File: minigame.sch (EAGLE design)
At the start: 37 parts, among them J1 AVR_SPI_PRG_6PTH, U1 MCP73831, U2 MIC5219 3.3V, Y1 8MHz

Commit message: ERC
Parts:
- LED1: value (none) -> RED
- OLED128X64: value (none) -> ADAFRUIT-938
- POWER: value (none) -> ON/OFF
- renumbered OLED128X64-938 to OLED128X64
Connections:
- removed net N$3: R1.1, S1.2, U$1.!RESET
- net GND: now also BAT1.-; no longer BAT1.+
- net RST: now also R1.1, S1.2, U$1.!RESET
- net VBAT: now also BAT1.+; no longer BAT1.-
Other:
- moved on the sheet: BAT1

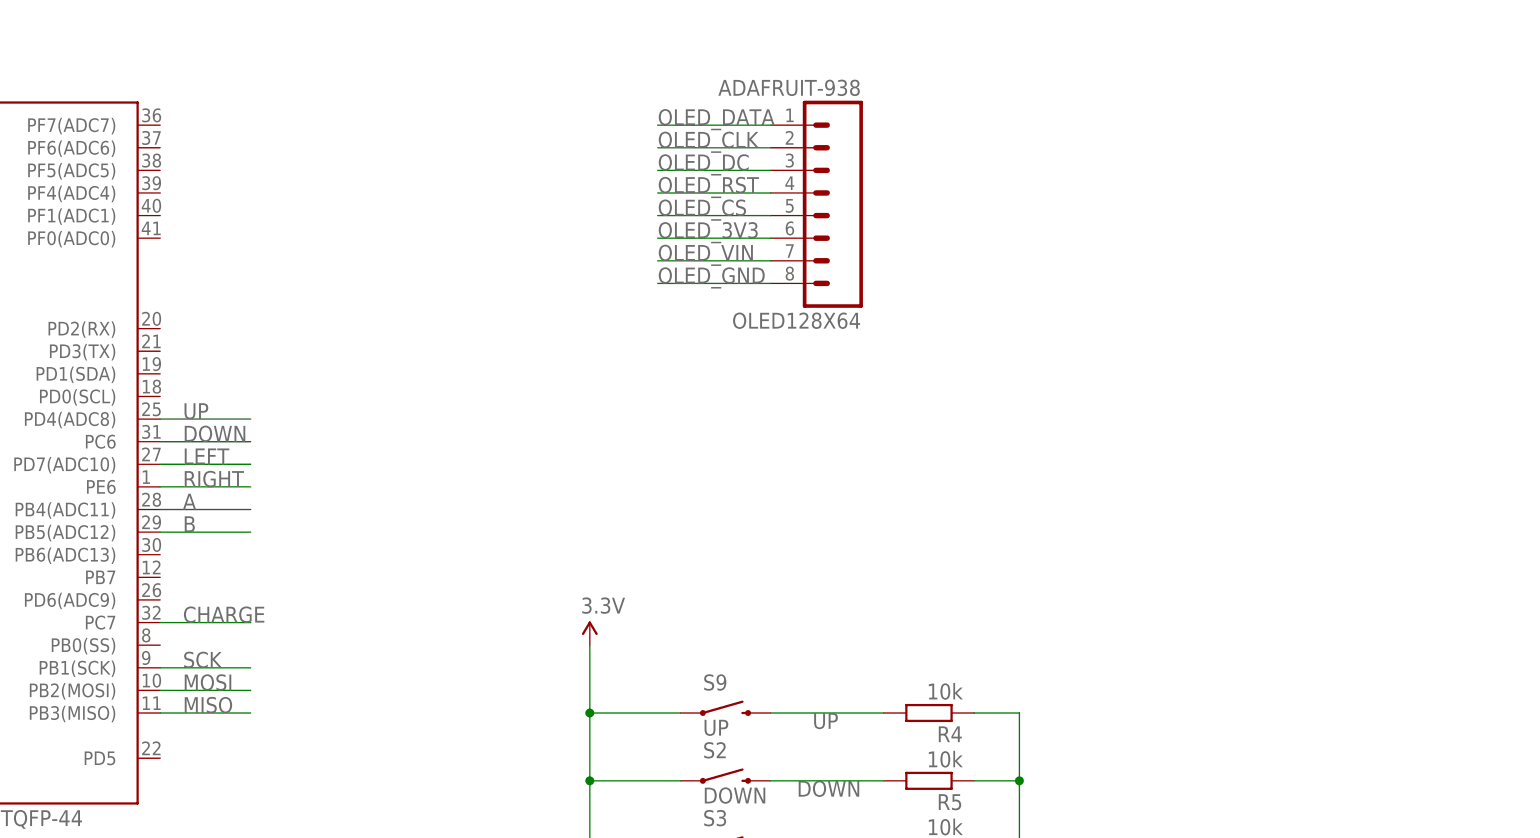
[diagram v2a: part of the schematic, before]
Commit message: Added OLED wires Added buzzer circuit
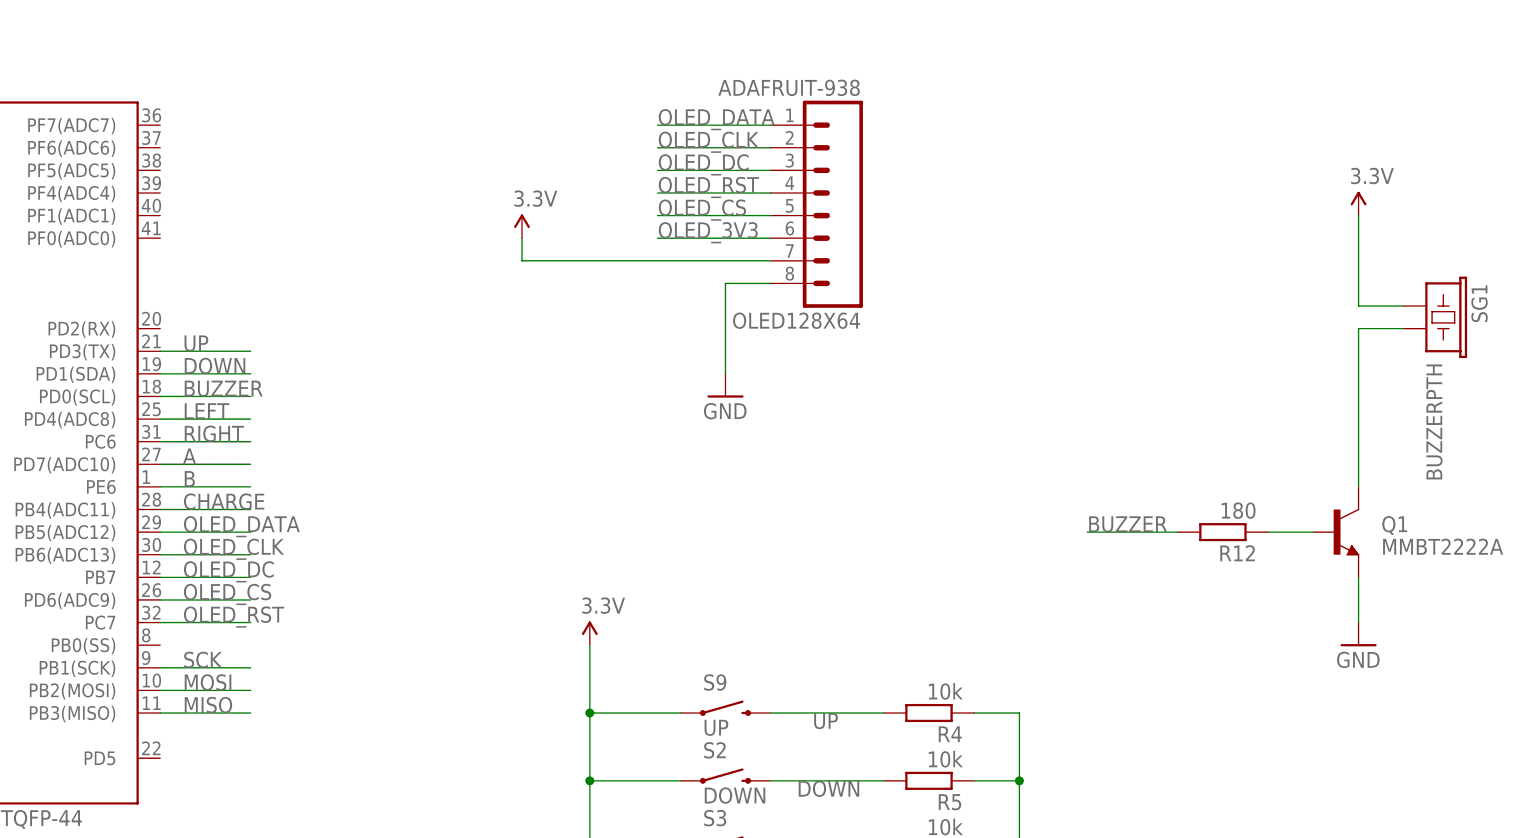
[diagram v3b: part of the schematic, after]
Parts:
- added Q1: MMBT2222A, SparkFun-DiscreteSemi:TRANSISTOR_NPNMMBT2222A
- added R12: 180, rcl:R-EU_M0805
- added SG1: BUZZERPTH, SparkFun-Electromechanical:BUZZERPTH
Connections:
- removed net OLED_GND: OLED128X64.8
- removed net OLED_VIN: OLED128X64.7
- new net BUZZER: R12.2, U$1.PD0(SCL)
- new net N$11: Q1.B, R12.1
- new net N$3: Q1.C, SG1.2
- net 3.3V: now also OLED128X64.7, SG1.1
- net A: now also U$1.PD7(ADC10); no longer U$1.PB4(ADC11)
- net B: now also U$1.PE6; no longer U$1.PB5(ADC12)
- net CHARGE: now also U$1.PB4(ADC11); no longer U$1.PC7
- net DOWN: now also U$1.PD1(SDA); no longer U$1.PC6
- net GND: now also OLED128X64.8, Q1.E
- net LEFT: now also U$1.PD4(ADC8); no longer U$1.PD7(ADC10)
- net OLED_CLK: now also U$1.PB6(ADC13)
- net OLED_CS: now also U$1.PD6(ADC9)
- net OLED_DATA: now also U$1.PB5(ADC12)
- net OLED_DC: now also U$1.PB7
- net OLED_RST: now also U$1.PC7
- net RIGHT: now also U$1.PC6; no longer U$1.PE6
- net UP: now also U$1.PD3(TX); no longer U$1.PD4(ADC8)
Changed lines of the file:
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@@
 <part name="U$1" library="SparkFun-DigitalIC" deviceset="ATMEGA32U4" device="TQFP-44"/>
 <part name="SUPPLY1" library="SparkFun-Aesthetics" deviceset="3.3V" device=""/>
-<part name="GND1" library="SparkFun-Aesthetics" deviceset="GND" device=""/>
+<part name="COPY+" library="SparkFun-Aesthetics" deviceset="GND" device=""/>
 <part name="JP1" library="SparkFun-Connectors" deviceset="USB" device="-SMD-NS"/>
 <part name="Y1" library="SparkFun-FreqCtrl" deviceset="CRYSTAL" device="HC49US" value="8MHz"/>
@@
 <part name="C9" library="SparkFun-Passives" deviceset="CAP" device="1206" value="0.1uF"/>
 <part name="SUPPLY5" library="SparkFun-Aesthetics" deviceset="3.3V" device=""/>
+<part name="COPY+1" library="SparkFun-Aesthetics" deviceset="GND" device=""/>
+<part name="SUPPLY6" library="SparkFun-Aesthetics" deviceset="3.3V" device=""/>
+<part name="SG1" library="SparkFun-Electromechanical" deviceset="BUZZER" device="PTH"/>
+<part name="Q1" library="SparkFun-DiscreteSemi" deviceset="TRANSISTOR_NPN" device="MMBT2222A" value="MMBT2222A"/>
+<part name="R12" library="rcl" deviceset="R-EU_" device="M0805" value="180"/>
+<part name="SUPPLY7" library="SparkFun-Aesthetics" deviceset="3.3V" device=""/>
+<part name="COPY+2" library="SparkFun-Aesthetics" deviceset="GND" device=""/>
 </parts>
 <sheets>
@@
 <instance part="U$1" gate="G$1" x="15.24" y="40.64"/>
 <instance part="SUPPLY1" gate="G$1" x="-30.48" y="99.06"/>
-<instance part="GND1" gate="1" x="-7.62" y="-10.16"/>
+<instance part="COPY+" gate="1" x="-7.62" y="-10.16"/>
 <instance part="JP1" gate="G$1" x="-81.28" y="76.2" rot="R180"/>
 <instance part="Y1" gate="G$1" x="-10.16" y="27.94" rot="R90"/>
@@
 <instance part="C9" gate="G$1" x="152.4" y="-76.2" rot="R180"/>
 <instance part="SUPPLY5" gate="G$1" x="152.4" y="-63.5"/>
+<instance part="COPY+1" gate="1" x="96.52" y="45.72"/>
+<instance part="SUPPLY6" gate="G$1" x="73.66" y="63.5"/>
+<instance part="SG1" gate="G$1" x="175.26" y="55.88" rot="R270"/>
+<instance part="Q1" gate="G$1" x="165.1" y="30.48"/>
+<instance part="R12" gate="G$1" x="152.4" y="30.48" rot="R180"/>
+<instance part="SUPPLY7" gate="G$1" x="167.64" y="66.04"/>
+<instance part="COPY+2" gate="1" x="167.64" y="17.78"/>
 </instances>
 <busses>
@@
 <junction x="-7.62" y="7.62"/>
 <junction x="-7.62" y="5.08"/>
-<pinref part="GND1" gate="1" pin="GND"/>
+<pinref part="COPY+" gate="1" pin="GND"/>
 <wire x1="-7.62" y1="-7.62" x2="-7.62" y2="2.54" width="0.1524" layer="91"/>
 <junction x="-7.62" y="2.54"/>
@@
 <wire x1="35.56" y1="-86.36" x2="35.56" y2="-93.98" width="0.1524" layer="91"/>
 </segment>
+<segment>
+<pinref part="COPY+1" gate="1" pin="GND"/>
+<wire x1="96.52" y1="48.26" x2="96.52" y2="58.42" width="0.1524" layer="91"/>
+<pinref part="OLED128X64" gate="G$1" pin="8"/>
+<wire x1="96.52" y1="58.42" x2="101.6" y2="58.42" width="0.1524" layer="91"/>
+</segment>
+<segment>
+<pinref part="COPY+2" gate="1" pin="GND"/>
+<pinref part="Q1" gate="G$1" pin="E"/>
+<wire x1="167.64" y1="20.32" x2="167.64" y2="25.4" width="0.1524" layer="91"/>
+</segment>
 </net>
 <net name="3.3V" class="0">
@@
 <junction x="152.4" y="-68.58"/>
 </segment>
+<segment>
+<pinref part="OLED128X64" gate="G$1" pin="7"/>
+<wire x1="101.6" y1="60.96" x2="73.66" y2="60.96" width="0.1524" layer="91"/>
+<pinref part="SUPPLY6" gate="G$1" pin="3.3V"/>
+<wire x1="73.66" y1="60.96" x2="73.66" y2="63.5" width="0.1524" layer="91"/>
+</segment>
+<segment>
+<pinref part="SUPPLY7" gate="G$1" pin="3.3V"/>
+<wire x1="167.64" y1="66.04" x2="167.64" y2="55.88" width="0.1524" layer="91"/>
+<pinref part="SG1" gate="G$1" pin="1"/>
+<wire x1="167.64" y1="55.88" x2="172.72" y2="55.88" width="0.1524" layer="91"/>
+</segment>
 </net>
 <net name="N$4" class="0">
@@
 <label x="88.9" y="76.2" size="1.778" layer="95"/>
 </segment>
+<segment>
+<pinref part="U$1" gate="G$1" pin="PB5(ADC12)"/>
+<wire x1="33.02" y1="30.48" x2="43.18" y2="30.48" width="0.1524" layer="91"/>
+<label x="35.56" y="30.48" size="1.778" layer="95"/>
+</segment>
 </net>
 <net name="OLED_CLK" class="0">
@@
 <label x="88.9" y="73.66" size="1.778" layer="95"/>
 </segment>
+<segment>
+<pinref part="U$1" gate="G$1" pin="PB6(ADC13)"/>
+<wire x1="33.02" y1="27.94" x2="43.18" y2="27.94" width="0.1524" layer="91"/>
+<label x="35.56" y="27.94" size="1.778" layer="95"/>
+</segment>
 </net>
 <net name="OLED_DC" class="0">
@@
 <label x="88.9" y="71.12" size="1.778" layer="95"/>
 </segment>
+<segment>
+<pinref part="U$1" gate="G$1" pin="PB7"/>
+<wire x1="33.02" y1="25.4" x2="43.18" y2="25.4" width="0.1524" layer="91"/>
+<label x="35.56" y="25.4" size="1.778" layer="95"/>
+</segment>
 </net>
 <net name="OLED_RST" class="0">
@@
 <label x="88.9" y="68.58" size="1.778" layer="95"/>
 </segment>
+<segment>
+<pinref part="U$1" gate="G$1" pin="PC7"/>
+<wire x1="33.02" y1="20.32" x2="43.18" y2="20.32" width="0.1524" layer="91"/>
+<label x="35.56" y="20.32" size="1.778" layer="95"/>
+</segment>
 </net>
 <net name="OLED_CS" class="0">
@@
 <label x="88.9" y="66.04" size="1.778" layer="95"/>
 </segment>
+<segment>
+<pinref part="U$1" gate="G$1" pin="PD6(ADC9)"/>
+<wire x1="33.02" y1="22.86" x2="43.18" y2="22.86" width="0.1524" layer="91"/>
+<label x="35.56" y="22.86" size="1.778" layer="95"/>
+</segment>
 </net>
 <net name="OLED_3V3" class="0">
@@
 <wire x1="101.6" y1="63.5" x2="88.9" y2="63.5" width="0.1524" layer="91"/>
 <label x="88.9" y="63.5" size="1.778" layer="95"/>
-</segment>
-</net>
-<net name="OLED_VIN" class="0">
-<segment>
-<pinref part="OLED128X64" gate="G$1" pin="7"/>
-<wire x1="101.6" y1="60.96" x2="88.9" y2="60.96" width="0.1524" layer="91"/>
-<label x="88.9" y="60.96" size="1.778" layer="95"/>
-</segment>
-</net>
-<net name="OLED_GND" class="0">
-<segment>
-<pinref part="OLED128X64" gate="G$1" pin="8"/>
-<wire x1="101.6" y1="58.42" x2="88.9" y2="58.42" width="0.1524" layer="91"/>
-<label x="88.9" y="58.42" size="1.778" layer="95"/>
 </segment>
 </net>
@@
 </segment>
 <segment>
-<pinref part="U$1" gate="G$1" pin="PD4(ADC8)"/>
-<wire x1="33.02" y1="43.18" x2="43.18" y2="43.18" width="0.1524" layer="91"/>
-<label x="35.56" y="43.18" size="1.778" layer="95"/>
+<pinref part="U$1" gate="G$1" pin="PD3(TX)"/>
+<wire x1="33.02" y1="50.8" x2="43.18" y2="50.8" width="0.1524" layer="91"/>
+<label x="35.56" y="50.8" size="1.778" layer="95"/>
 </segment>
 </net>
@@
 </segment>
 <segment>
-<pinref part="U$1" gate="G$1" pin="PC6"/>
-<wire x1="33.02" y1="40.64" x2="43.18" y2="40.64" width="0.1524" layer="91"/>
-<label x="35.56" y="40.64" size="1.778" layer="95"/>
+<pinref part="U$1" gate="G$1" pin="PD1(SDA)"/>
+<wire x1="33.02" y1="48.26" x2="43.18" y2="48.26" width="0.1524" layer="91"/>
+<label x="35.56" y="48.26" size="1.778" layer="95"/>
 </segment>
 </net>
@@
 </segment>
 <segment>
-<pinref part="U$1" gate="G$1" pin="PD7(ADC10)"/>
-<wire x1="33.02" y1="38.1" x2="43.18" y2="38.1" width="0.1524" layer="91"/>
-<label x="35.56" y="38.1" size="1.778" layer="95"/>
+<pinref part="U$1" gate="G$1" pin="PD4(ADC8)"/>
+<wire x1="33.02" y1="43.18" x2="43.18" y2="43.18" width="0.1524" layer="91"/>
+<label x="35.56" y="43.18" size="1.778" layer="95"/>
 </segment>
 </net>
@@
 </segment>
 <segment>
-<pinref part="U$1" gate="G$1" pin="PE6"/>
-<wire x1="33.02" y1="35.56" x2="43.18" y2="35.56" width="0.1524" layer="91"/>
-<label x="35.56" y="35.56" size="1.778" layer="95"/>
+<pinref part="U$1" gate="G$1" pin="PC6"/>
+<wire x1="33.02" y1="40.64" x2="43.18" y2="40.64" width="0.1524" layer="91"/>
+<label x="35.56" y="40.64" size="1.778" layer="95"/>
 </segment>
 </net>
@@
 </segment>
 <segment>
-<pinref part="U$1" gate="G$1" pin="PB4(ADC11)"/>
-<wire x1="33.02" y1="33.02" x2="43.18" y2="33.02" width="0.1524" layer="91"/>
-<label x="35.56" y="33.02" size="1.778" layer="95"/>
+<pinref part="U$1" gate="G$1" pin="PD7(ADC10)"/>
+<wire x1="33.02" y1="38.1" x2="43.18" y2="38.1" width="0.1524" layer="91"/>
+<label x="35.56" y="38.1" size="1.778" layer="95"/>
 </segment>
 </net>
@@
 </segment>
 <segment>
-<pinref part="U$1" gate="G$1" pin="PB5(ADC12)"/>
-<wire x1="33.02" y1="30.48" x2="43.18" y2="30.48" width="0.1524" layer="91"/>
-<label x="35.56" y="30.48" size="1.778" layer="95"/>
+<pinref part="U$1" gate="G$1" pin="PE6"/>
+<wire x1="33.02" y1="35.56" x2="43.18" y2="35.56" width="0.1524" layer="91"/>
+<label x="35.56" y="35.56" size="1.778" layer="95"/>
 </segment>
 </net>
@@
 </net>
 <net name="CHARGE" class="0">
-<segment>
-<pinref part="U$1" gate="G$1" pin="PC7"/>
-<wire x1="33.02" y1="20.32" x2="43.18" y2="20.32" width="0.1524" layer="91"/>
-<label x="35.56" y="20.32" size="1.778" layer="95"/>
-</segment>
 <segment>
 <pinref part="U1" gate="G$1" pin="STAT"/>
@@
 <junction x="-25.4" y="-33.02"/>
 <label x="-22.86" y="-33.02" size="1.778" layer="95"/>
+</segment>
+<segment>
+<pinref part="U$1" gate="G$1" pin="PB4(ADC11)"/>
+<wire x1="33.02" y1="33.02" x2="43.18" y2="33.02" width="0.1524" layer="91"/>
+<label x="35.56" y="33.02" size="1.778" layer="95"/>
 </segment>
 </net>
@@
 </segment>
 </net>
+<net name="N$3" class="0">
+<segment>
+<pinref part="SG1" gate="G$1" pin="2"/>
+<wire x1="172.72" y1="53.34" x2="167.64" y2="53.34" width="0.1524" layer="91"/>
+<pinref part="Q1" gate="G$1" pin="C"/>
+<wire x1="167.64" y1="53.34" x2="167.64" y2="35.56" width="0.1524" layer="91"/>
+</segment>
+</net>
+<net name="N$11" class="0">
+<segment>
+<pinref part="R12" gate="G$1" pin="1"/>
+<pinref part="Q1" gate="G$1" pin="B"/>
+<wire x1="157.48" y1="30.48" x2="162.56" y2="30.48" width="0.1524" layer="91"/>
+</segment>
+</net>
+<net name="BUZZER" class="0">
+<segment>
+<pinref part="U$1" gate="G$1" pin="PD0(SCL)"/>
+<wire x1="33.02" y1="45.72" x2="43.18" y2="45.72" width="0.1524" layer="91"/>
+<label x="35.56" y="45.72" size="1.778" layer="95"/>
+</segment>
+<segment>
+<pinref part="R12" gate="G$1" pin="2"/>
+<wire x1="147.32" y1="30.48" x2="137.16" y2="30.48" width="0.1524" layer="91"/>
+<label x="137.16" y="30.48" size="1.778" layer="95"/>
+</segment>
+</net>

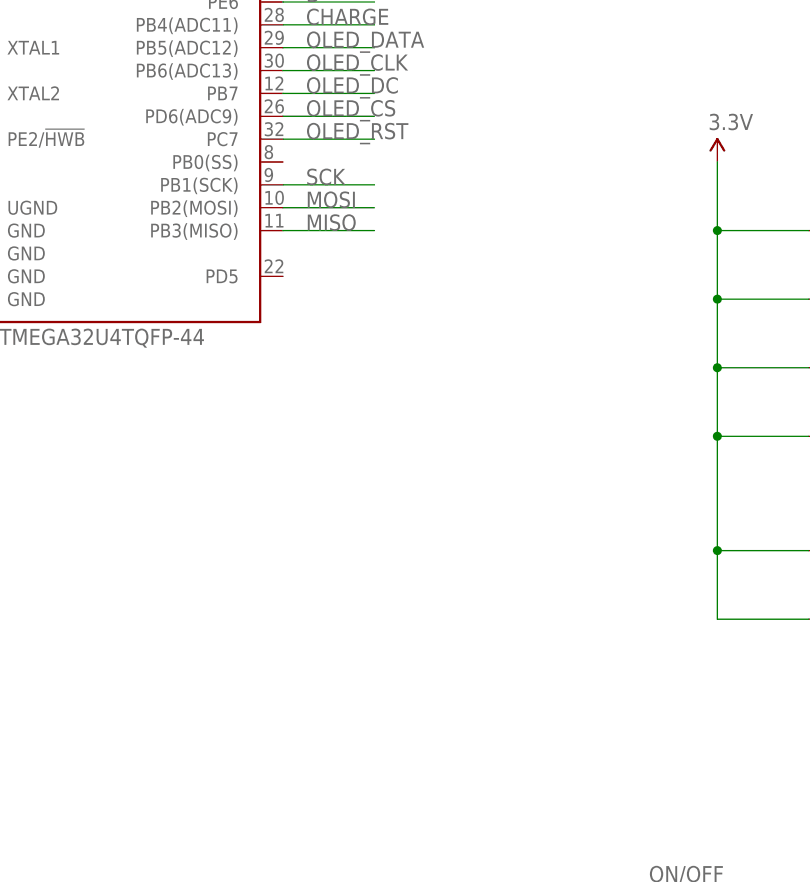
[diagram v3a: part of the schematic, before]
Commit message: Added RX/TX LEDs
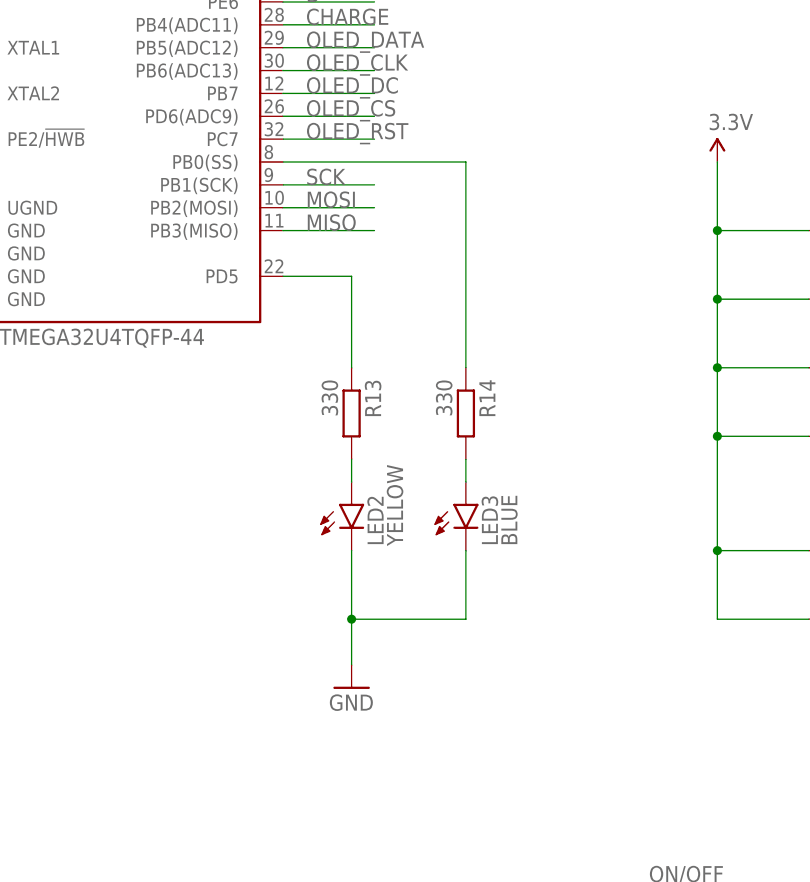
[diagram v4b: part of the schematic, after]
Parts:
- added LED2: YELLOW, SparkFun-LED:LED0603
- added LED3: BLUE, SparkFun-LED:LED0603
- added R13, R14: 330, rcl:R-EU_M0805
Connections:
- new net N$12: LED2.A, R13.2
- new net N$13: LED3.A, R14.2
- new net N$15: R13.1, U$1.PD5
- new net N$16: R14.1, U$1.PB0(SS)
- net GND: now also LED2.C, LED3.C
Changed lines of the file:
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@@
 <part name="SUPPLY7" library="SparkFun-Aesthetics" deviceset="3.3V" device=""/>
 <part name="COPY+2" library="SparkFun-Aesthetics" deviceset="GND" device=""/>
+<part name="LED2" library="SparkFun-LED" deviceset="LED" device="0603" value="YELLOW"/>
+<part name="LED3" library="SparkFun-LED" deviceset="LED" device="0603" value="BLUE"/>
+<part name="R13" library="rcl" deviceset="R-EU_" device="M0805" value="330"/>
+<part name="R14" library="rcl" deviceset="R-EU_" device="M0805" value="330"/>
+<part name="GND1" library="SparkFun-Aesthetics" deviceset="GND" device=""/>
 </parts>
 <sheets>
@@
 <instance part="SUPPLY7" gate="G$1" x="167.64" y="66.04"/>
 <instance part="COPY+2" gate="1" x="167.64" y="17.78"/>
+<instance part="LED2" gate="G$1" x="40.64" y="-20.32"/>
+<instance part="LED3" gate="G$1" x="53.34" y="-20.32"/>
+<instance part="R13" gate="G$1" x="40.64" y="-10.16" rot="R270"/>
+<instance part="R14" gate="G$1" x="53.34" y="-10.16" rot="R270"/>
+<instance part="GND1" gate="1" x="40.64" y="-40.64"/>
 </instances>
 <busses>
@@
 <wire x1="167.64" y1="20.32" x2="167.64" y2="25.4" width="0.1524" layer="91"/>
 </segment>
+<segment>
+<pinref part="LED2" gate="G$1" pin="C"/>
+<wire x1="40.64" y1="-25.4" x2="40.64" y2="-33.02" width="0.1524" layer="91"/>
+<wire x1="40.64" y1="-33.02" x2="53.34" y2="-33.02" width="0.1524" layer="91"/>
+<pinref part="LED3" gate="G$1" pin="C"/>
+<wire x1="53.34" y1="-33.02" x2="53.34" y2="-25.4" width="0.1524" layer="91"/>
+<pinref part="GND1" gate="1" pin="GND"/>
+<wire x1="40.64" y1="-38.1" x2="40.64" y2="-33.02" width="0.1524" layer="91"/>
+<junction x="40.64" y="-33.02"/>
+</segment>
 </net>
 <net name="3.3V" class="0">
@@
 </segment>
 </net>
+<net name="N$12" class="0">
+<segment>
+<pinref part="R13" gate="G$1" pin="2"/>
+<pinref part="LED2" gate="G$1" pin="A"/>
+<wire x1="40.64" y1="-15.24" x2="40.64" y2="-17.78" width="0.1524" layer="91"/>
+</segment>
+</net>
+<net name="N$13" class="0">
+<segment>
+<pinref part="R14" gate="G$1" pin="2"/>
+<pinref part="LED3" gate="G$1" pin="A"/>
+<wire x1="53.34" y1="-15.24" x2="53.34" y2="-17.78" width="0.1524" layer="91"/>
+</segment>
+</net>
+<net name="N$15" class="0">
+<segment>
+<pinref part="U$1" gate="G$1" pin="PD5"/>
+<pinref part="R13" gate="G$1" pin="1"/>
+<wire x1="33.02" y1="5.08" x2="40.64" y2="5.08" width="0.1524" layer="91"/>
+<wire x1="40.64" y1="5.08" x2="40.64" y2="-5.08" width="0.1524" layer="91"/>
+</segment>
+</net>
+<net name="N$16" class="0">
+<segment>
+<pinref part="U$1" gate="G$1" pin="PB0(SS)"/>
+<pinref part="R14" gate="G$1" pin="1"/>
+<wire x1="33.02" y1="17.78" x2="53.34" y2="17.78" width="0.1524" layer="91"/>
+<wire x1="53.34" y1="17.78" x2="53.34" y2="-5.08" width="0.1524" layer="91"/>
+</segment>
+</net>

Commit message: Preliminary components placement
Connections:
- removed net OLED_3V3: OLED128X64.6
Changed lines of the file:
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@@
-</segment>
-</net>
-<net name="OLED_3V3" class="0">
-<segment>
-<pinref part="OLED128X64" gate="G$1" pin="6"/>
-<wire x1="101.6" y1="63.5" x2="88.9" y2="63.5" width="0.1524" layer="91"/>
-<label x="88.9" y="63.5" size="1.778" layer="95"/>
 </segment>
 </net>
